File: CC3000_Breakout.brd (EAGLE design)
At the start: 20.8 x 36.8 mm, 18 parts

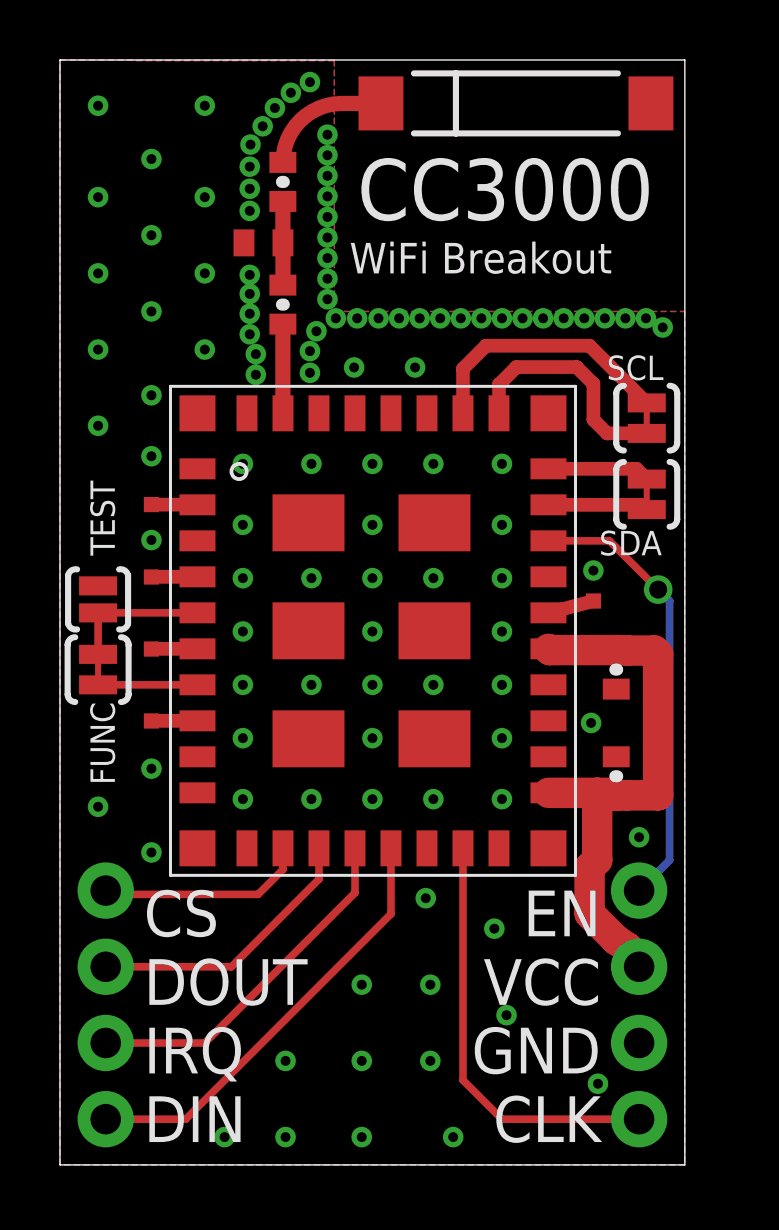
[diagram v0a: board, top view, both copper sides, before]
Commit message: Version 1.3
The antenna in Matt's design wasn't the right size, I've fixed the
antenna footprint to match the actual chip used.
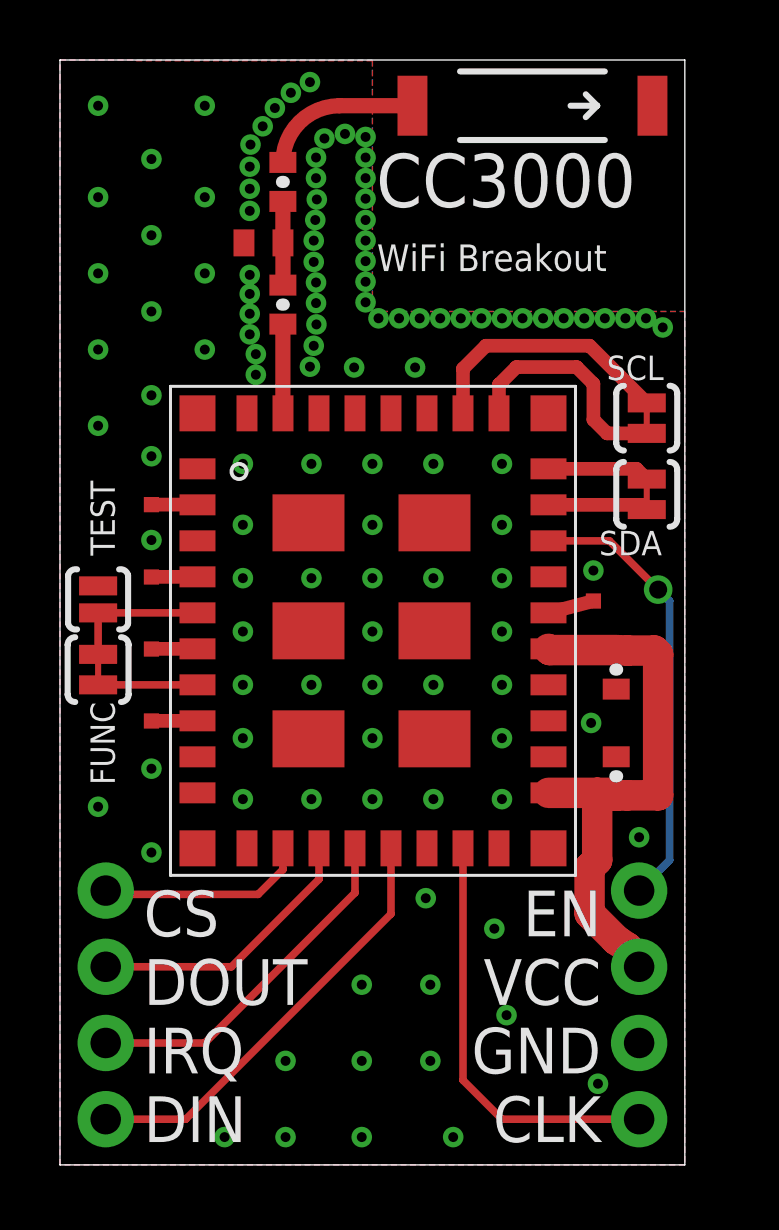
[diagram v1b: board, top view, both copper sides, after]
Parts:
- U$3: value ANTENNA2SMD2 -> ANTENNA2SMD5; device SparkFun:ANTENNA-CHIP3 -> SparkFun-RF-Modified:ANTENNA-CHIP5
- moved U$3 0.56 mm to (15.7, 35.3), turned to 0 degrees
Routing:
- net N$15: track 4.08 -> 5.10 mm
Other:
- board text added: "V1.3"
- board text removed: "V1.2"
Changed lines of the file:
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@@
 <setting verticaltext="up"/>
 </settings>
-<grid distance="0.01" unitdist="inch" unit="inch" style="lines" multiple="1" display="yes" altdistance="0.025" altunitdist="inch" altunit="inch"/>
+<grid distance="0.05" unitdist="inch" unit="inch" style="lines" multiple="1" display="yes" altdistance="0.025" altunitdist="inch" altunit="inch"/>
 <layers>
 <layer number="1" name="Top" color="4" fill="1" visible="yes" active="yes"/>
@@
 <text x="18.034" y="4.572" size="1.524" layer="25" rot="R180">GND</text>
 <text x="18.034" y="2.286" size="1.524" layer="25" rot="R180">CLK</text>
-<text x="9.906" y="31.496" size="2.032" layer="25">CC3000</text>
+<text x="10.541" y="31.9278" size="1.778" layer="25">CC3000</text>
 <text x="15.24" y="0.762" size="2.032" layer="26" rot="MR90">CC3000 Breakout</text>
-<text x="13.208" y="0.762" size="1.4224" layer="26" rot="MR90">V1.2</text>
+<text x="13.208" y="0.762" size="1.4224" layer="26" rot="MR90">V1.3</text>
 <text x="9.398" y="0.762" size="2.032" layer="26" rot="MR90">(C)2013 Bubbletronics</text>
 <text x="6.604" y="0.762" size="1.778" layer="26" rot="MR90">CC by NC SA</text>
 <text x="3.048" y="0.762" size="1.9304" layer="26" rot="MR90">bubbletronics.com</text>
-<text x="9.652" y="29.718" size="1.016" layer="25">WiFi Breakout</text>
+<text x="10.5664" y="29.7942" size="0.889" layer="25">WiFi Breakout</text>
 </plain>
 <attributes>
@@
 <attribute name="VALUE" x="5.207" y="30.0863" size="0.4064" layer="27" rot="R90"/>
 </element>
-<element name="U$3" library="SparkFun" package="ANTENNA-CHIP3" value="ANTENNA2SMD2" x="15.198090625" y="35.3822" rot="R90"/>
 <element name="FUNC" library="SparkFun-Passives" package="SJ_2S-TRACE" value="SOLDERJUMPERTRACE" x="1.27" y="16.51" smashed="yes" rot="R270">
 <attribute name="NAME" x="1.016" y="15.4305" size="0.8128" layer="25" rot="R270"/>
@@
 <element name="JP1" library="SparkFun-Connectors" package="1X04" value="Jumper1" x="1.524" y="1.524" smashed="yes" rot="R90"/>
 <element name="JP2" library="SparkFun-Connectors" package="1X04" value="Jumper2" x="19.304" y="9.144" smashed="yes" rot="R270"/>
+<element name="U$3" library="SparkFun-RF-Modified" package="ANTENNA-CHIP5" value="ANTENNA2SMD5" x="15.748" y="35.306" smashed="yes"/>
 </elements>
 <signals>
@@
 <vertex x="2.54" y="36.83"/>
 <vertex x="2.54" y="36.8046"/>
-<vertex x="9.144" y="36.8046"/>
-<vertex x="9.144" y="28.448"/>
+<vertex x="10.414" y="36.8046"/>
+<vertex x="10.414" y="28.448"/>
 <vertex x="20.828" y="28.448"/>
 <vertex x="20.828" y="0"/>
@@
 <vertex x="0" y="0"/>
 <vertex x="0" y="36.83"/>
-<vertex x="9.144" y="36.83"/>
-<vertex x="9.144" y="28.448"/>
+<vertex x="10.414" y="36.83"/>
+<vertex x="10.414" y="28.448"/>
 <vertex x="20.828" y="28.448"/>
 <vertex x="20.828" y="0"/>
 </polygon>
-<via x="8.3312" y="26.4033" extent="1-16" drill="0.3302" diameter="0.0254"/>
-<via x="8.5471" y="27.7876" extent="1-16" drill="0.3302" diameter="0.0254"/>
-<via x="9.1948" y="28.2194" extent="1-16" drill="0.3302" diameter="0.0254"/>
+<via x="8.3312" y="26.6065" extent="1-16" drill="0.3302" diameter="0.0254"/>
+<via x="8.5471" y="28.0162" extent="1-16" drill="0.3302" diameter="0.0254"/>
+<via x="10.1854" y="29.4386" extent="1-16" drill="0.3302" diameter="0.0254"/>
 <via x="6.3246" y="31.8008" extent="1-16" drill="0.3302" diameter="0.0254"/>
-<via x="8.9154" y="34.3408" extent="1-16" drill="0.3302" diameter="0.0254"/>
-<via x="8.3312" y="27.1272" extent="1-16" drill="0.3302" diameter="0.0254"/>
-<via x="8.9154" y="30.226" extent="1-16" drill="0.3302" diameter="0.0254"/>
-<via x="8.9154" y="31.5976" extent="1-16" drill="0.3302" diameter="0.0254"/>
-<via x="8.9154" y="30.9118" extent="1-16" drill="0.3302" diameter="0.0254"/>
+<via x="9.4996" y="34.3662" extent="1-16" drill="0.3302" diameter="0.0254"/>
+<via x="8.4582" y="27.305" extent="1-16" drill="0.3302" diameter="0.0254"/>
+<via x="10.1854" y="31.496" extent="1-16" drill="0.3302" diameter="0.0254"/>
+<via x="10.1854" y="32.893" extent="1-16" drill="0.3302" diameter="0.0254"/>
+<via x="10.1854" y="32.2072" extent="1-16" drill="0.3302" diameter="0.0254"/>
 <via x="6.3246" y="27.686" extent="1-16" drill="0.3302" diameter="0.0254"/>
-<via x="8.9154" y="33.655" extent="1-16" drill="0.3302" diameter="0.0254"/>
-<via x="8.9154" y="29.5402" extent="1-16" drill="0.3302" diameter="0.0254"/>
+<via x="8.8138" y="34.2138" extent="1-16" drill="0.3302" diameter="0.0254"/>
+<via x="10.1854" y="30.8102" extent="1-16" drill="0.3302" diameter="0.0254"/>
 <via x="6.35" y="34.0106" extent="1-16" drill="0.3302" diameter="0.0254"/>
 <via x="6.3246" y="33.274" extent="1-16" drill="0.3302" diameter="0.0254"/>
@@
 <via x="6.5278" y="27.0256" extent="1-16" drill="0.3302" diameter="0.0254"/>
 <via x="8.3312" y="36.0934" extent="1-16" drill="0.3302" diameter="0.0254"/>
-<via x="8.9154" y="28.8544" extent="1-16" drill="0.3302" diameter="0.0254"/>
+<via x="10.1854" y="30.1244" extent="1-16" drill="0.3302" diameter="0.0254"/>
 <via x="7.1628" y="35.2298" extent="1-16" drill="0.3302" diameter="0.0254"/>
 <via x="6.5278" y="26.3398" extent="1-16" drill="0.3302" diameter="0.0254"/>
 <via x="6.3246" y="29.0322" extent="1-16" drill="0.3302" diameter="0.0254"/>
-<via x="8.9154" y="32.9692" extent="1-16" drill="0.3302" diameter="0.0254"/>
-<via x="8.9154" y="32.2834" extent="1-16" drill="0.3302" diameter="0.0254"/>
+<via x="10.1854" y="34.2646" extent="1-16" drill="0.3302" diameter="0.0254"/>
+<via x="10.1854" y="33.5788" extent="1-16" drill="0.3302" diameter="0.0254"/>
 <via x="6.3246" y="28.3718" extent="1-16" drill="0.3302" diameter="0.0254"/>
-<via x="9.906" y="28.2194" extent="1-16" drill="0.3302" diameter="0.0254"/>
+<via x="10.1854" y="28.7528" extent="1-16" drill="0.3302" diameter="0.0254"/>
 <via x="10.6172" y="28.2194" extent="1-16" drill="0.3302" diameter="0.0254"/>
 <via x="11.303" y="28.2194" extent="1-16" drill="0.3302" diameter="0.0254"/>
@@
 <via x="14.8844" y="4.9911" extent="1-16" drill="0.3302" diameter="0.0254"/>
 <via x="17.9324" y="2.7051" extent="1-16" drill="0.3302" diameter="0.0254"/>
+<via x="8.5344" y="33.5788" extent="1-16" drill="0.3302" diameter="0.0254"/>
+<via x="8.5344" y="32.893" extent="1-16" drill="0.3302" diameter="0.0254"/>
+<via x="8.5598" y="32.1818" extent="1-16" drill="0.3302" diameter="0.0254"/>
+<via x="8.509" y="31.496" extent="1-16" drill="0.3302" diameter="0.0254"/>
+<via x="8.4582" y="30.8102" extent="1-16" drill="0.3302" diameter="0.0254"/>
+<via x="8.4582" y="30.099" extent="1-16" drill="0.3302" diameter="0.0254"/>
+<via x="8.5344" y="29.4132" extent="1-16" drill="0.3302" diameter="0.0254"/>
+<via x="8.5344" y="28.7274" extent="1-16" drill="0.3302" diameter="0.0254"/>
 </signal>
 <signal name="SPI_CLK">
@@
 <contactref element="C1" pad="1"/>
 <contactref element="U$3" pad="FEED"/>
-<wire x1="10.698090625" y1="35.3822" x2="9.3957" y2="35.3822" width="0.508" layer="1"/>
-<wire x1="9.3957" y1="35.3822" x2="7.4295" y2="33.416" width="0.508" layer="1" curve="90"/>
+<wire x1="11.748" y1="35.306" x2="9.3195" y2="35.306" width="0.508" layer="1"/>
+<wire x1="9.3195" y1="35.306" x2="7.4295" y2="33.416" width="0.508" layer="1" curve="90"/>
 </signal>
 <signal name="N$14" class="3">
@@
 </signal>
 </signals>
-<errors>
-</errors>
 </board>
 </drawing>

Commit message: Abandoned project!
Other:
- board text added: "V1.4"
- board text removed: "V1.3"
